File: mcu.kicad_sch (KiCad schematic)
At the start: 16 parts, among them J301 Conn_PIC_ICSP_ICD, U301 LM4040DBZ-2.0, U302 PIC18F24K42

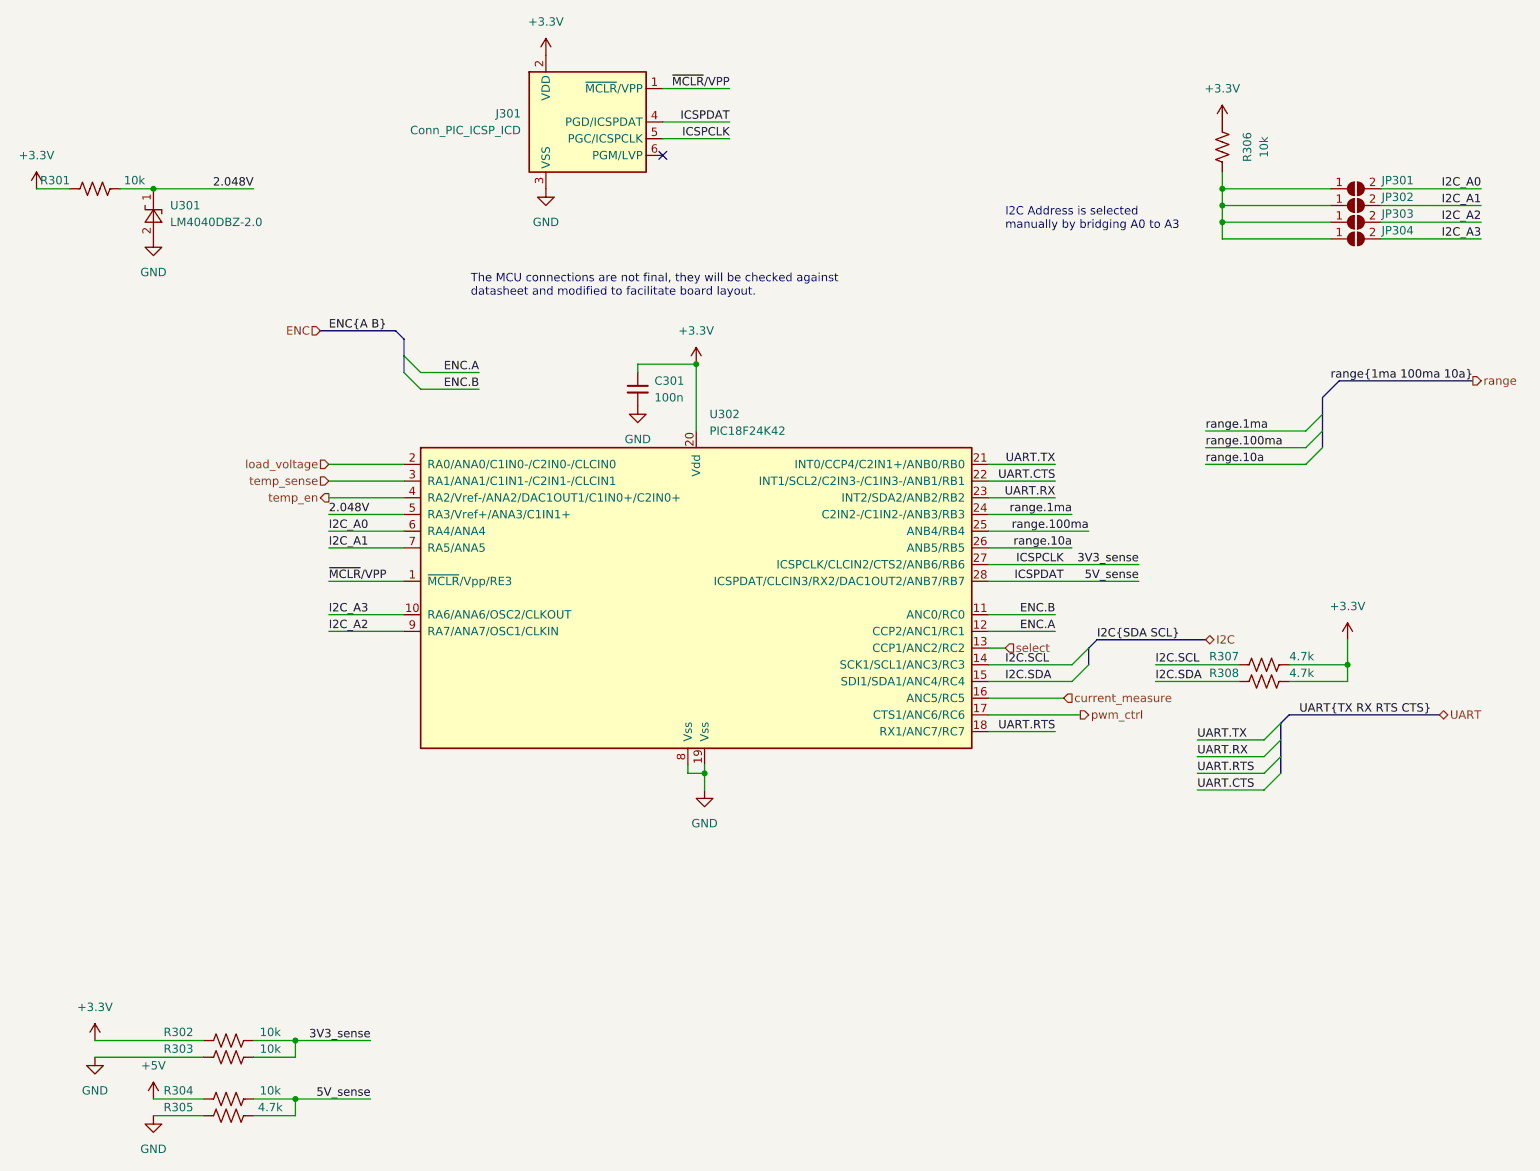
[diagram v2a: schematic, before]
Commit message: Add partnumbers
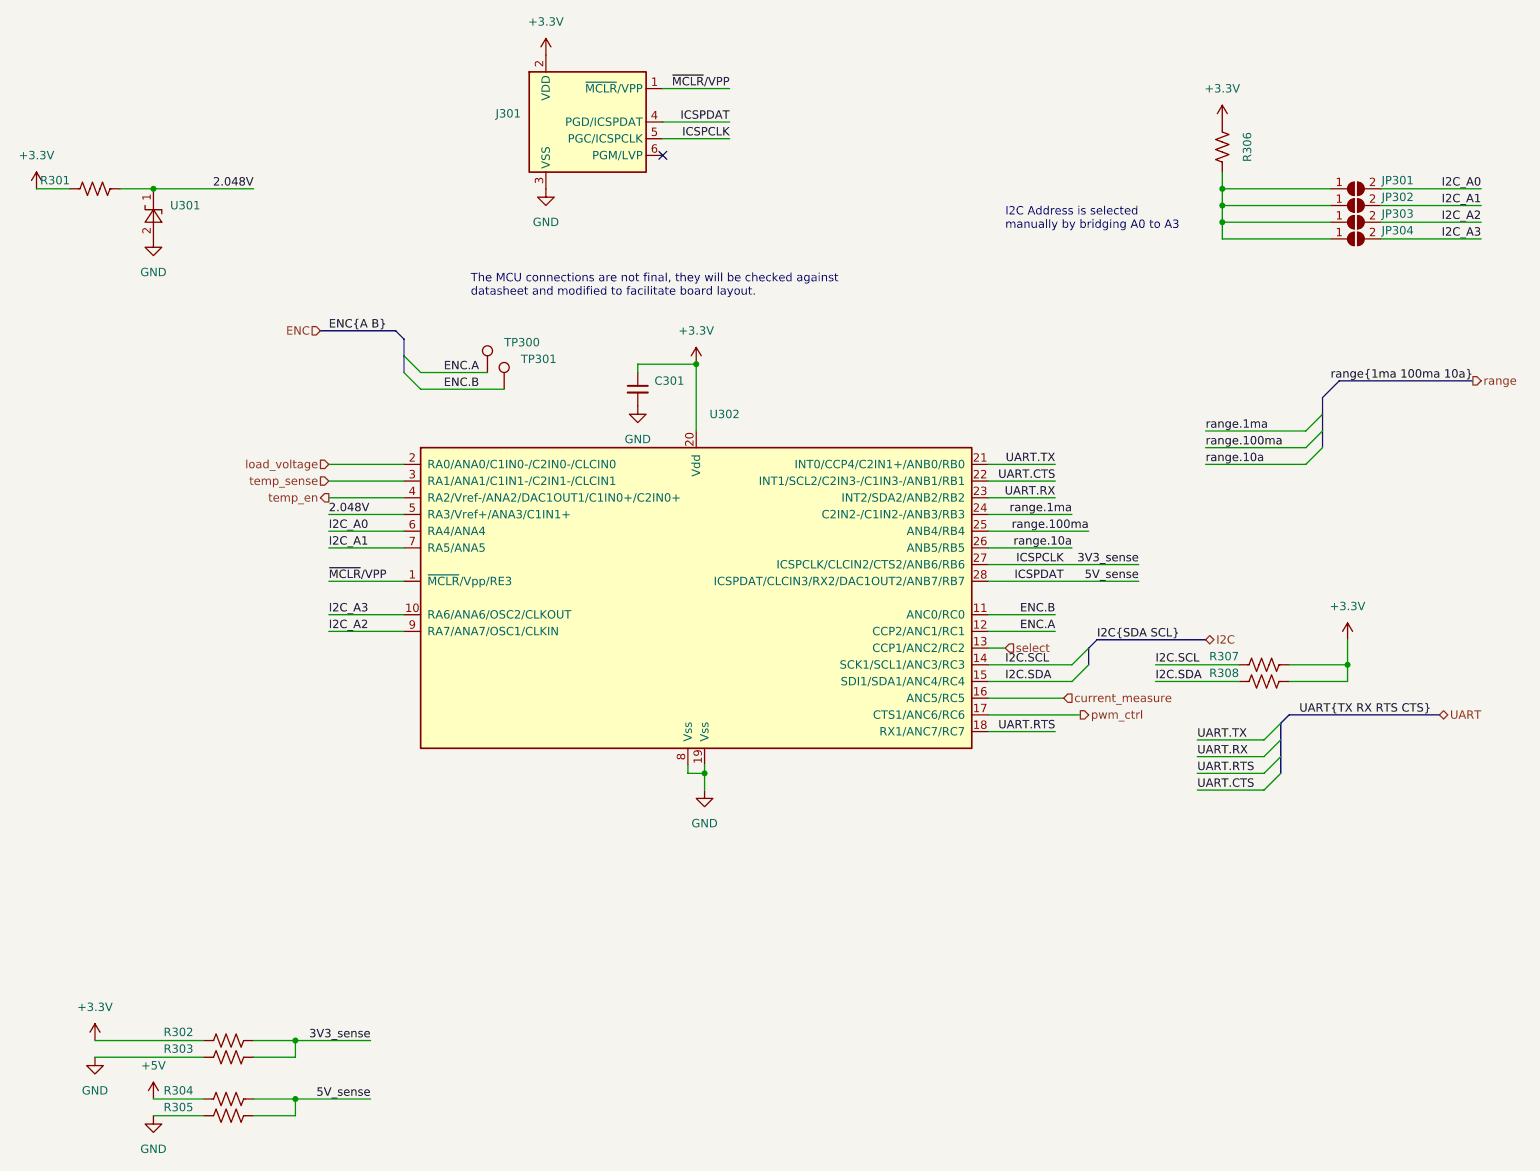
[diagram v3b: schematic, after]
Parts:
- added TP300, TP301: (no value), symbol Connector:TestPoint
- C301: value 100n -> (none); footprint Capacitor_SMD:C_0402_1005Metric -> (none); Manufacturer (none) -> Generic; PartNumber (none) -> Generic
- J301: value Conn_PIC_ICSP_ICD -> (none); footprint Connector_PinHeader_2.54mm:PinHeader_1x06_P2.54mm_Vertical -> (none); Manufacturer (none) -> Generic; PartNumber (none) -> Generic
- JP301, JP302, JP303, JP304: value SB -> (none); footprint Jumper:SolderJumper-2_P1.3mm_Open_TrianglePad1.0x1.5mm -> (none); Manufacturer (none) -> N.A.; PartNumber (none) -> N.A.
- R301, R302, R303, R304, R306: value 10k -> (none); footprint Resistor_SMD:R_0805_2012Metric -> (none); Manufacturer (none) -> Generic; PartNumber (none) -> Generic
- R305, R307, R308: value 4.7k -> (none); footprint Resistor_SMD:R_0805_2012Metric -> (none); Manufacturer (none) -> Generic; PartNumber (none) -> Generic
- U301: value LM4040DBZ-2.0 -> (none); footprint Package_TO_SOT_SMD:SOT-23 -> (none); Manufacturer (none) -> Texas Instruments; PartNumber (none) -> LM4040DBZ-2.0
- U302: value PIC18F24K42 -> (none); footprint Package_SO:SSOP-28_5.3x10.2mm_P0.65mm -> (none)
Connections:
- net ENC.A: now also TP300.1
- net ENC.B: now also TP301.1

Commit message: Fix missing footprints in schematic
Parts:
- C301, J301, JP301, JP302, JP303, JP304, R301, R302, R303, R304, R305, R306, R307, R308, TP300, TP301: now left out of the parts list
- U301: PartNumber LM4040DBZ-2.0 -> LM4040C20IDBZ
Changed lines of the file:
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@@
   )
   (symbol (lib_id "Device:R_US") (at 228.6 115.57 270) (unit 1)
-    (in_bom yes) (on_board yes)
+    (in_bom no) (on_board yes)
     (property "Reference" "R308" (id 0) (at 224.79 114.3 90)
       (effects (font (size 1.27 1.27)) (justify right))
@@
   )
   (symbol (lib_id "Device:R_US") (at 50.8 40.64 270) (unit 1)
-    (in_bom yes) (on_board yes)
+    (in_bom no) (on_board yes)
     (property "Reference" "R301" (id 0) (at 46.99 39.37 90)
       (effects (font (size 1.27 1.27)) (justify right))
@@
   )
   (symbol (lib_id "Connector:TestPoint") (at 110.49 68.58 0) (unit 1)
-    (in_bom yes) (on_board yes) (fields_autoplaced)
+    (in_bom no) (on_board yes) (fields_autoplaced)
     (property "Reference" "TP300" (id 0) (at 113.03 64.0079 0)
       (effects (font (size 1.27 1.27)) (justify left))
@@
   )
   (symbol (lib_id "Connector:Conn_PIC_ICSP_ICD") (at 124.46 30.48 0) (unit 1)
-    (in_bom yes) (on_board yes) (fields_autoplaced)
+    (in_bom no) (on_board yes) (fields_autoplaced)
     (property "Reference" "J301" (id 0) (at 115.57 29.2099 0)
       (effects (font (size 1.27 1.27)) (justify right))
@@
   )
   (symbol (lib_id "Device:R_US") (at 71.12 170.18 270) (unit 1)
-    (in_bom yes) (on_board yes)
+    (in_bom no) (on_board yes)
     (property "Reference" "R302" (id 0) (at 63.5 168.91 90))
     (property "Value" "" (id 1) (at 77.47 168.91 90))
@@
   )
   (symbol (lib_id "Jumper:SolderJumper_2_Open") (at 242.57 40.64 0) (unit 1)
-    (in_bom yes) (on_board yes)
+    (in_bom no) (on_board yes)
     (property "Reference" "JP301" (id 0) (at 248.92 39.37 0))
     (property "Value" "" (id 1) (at 242.57 36.83 0)
@@
   )
   (symbol (lib_id "Device:R_US") (at 71.12 172.72 90) (unit 1)
-    (in_bom yes) (on_board yes)
+    (in_bom no) (on_board yes)
     (property "Reference" "R303" (id 0) (at 63.5 171.45 90))
     (property "Value" "" (id 1) (at 77.47 171.45 90))
@@
   )
   (symbol (lib_id "Connector:TestPoint") (at 113.03 71.12 0) (unit 1)
-    (in_bom yes) (on_board yes) (fields_autoplaced)
+    (in_bom no) (on_board yes) (fields_autoplaced)
     (property "Reference" "TP301" (id 0) (at 115.57 66.5479 0)
       (effects (font (size 1.27 1.27)) (justify left))
@@
   )
   (symbol (lib_id "Device:R_US") (at 71.12 179.07 270) (unit 1)
-    (in_bom yes) (on_board yes)
+    (in_bom no) (on_board yes)
     (property "Reference" "R304" (id 0) (at 63.5 177.8 90))
     (property "Value" "" (id 1) (at 77.47 177.8 90))
@@
       (effects (font (size 1.27 1.27)) hide)
     )
-    (property "PartNumber" "LM4040DBZ-2.0" (id 5) (at 59.69 44.45 0)
+    (property "PartNumber" "LM4040C20IDBZ" (id 5) (at 59.69 44.45 0)
       (effects (font (size 1.27 1.27)) hide)
     )
@@
   )
   (symbol (lib_id "Device:C_Small") (at 133.35 71.12 0) (unit 1)
-    (in_bom yes) (on_board yes) (fields_autoplaced)
+    (in_bom no) (on_board yes) (fields_autoplaced)
     (property "Reference" "C301" (id 0) (at 135.89 69.8562 0)
       (effects (font (size 1.27 1.27)) (justify left))
@@
   )
   (symbol (lib_id "Device:R_US") (at 222.25 34.29 180) (unit 1)
-    (in_bom yes) (on_board yes)
+    (in_bom no) (on_board yes)
     (property "Reference" "R306" (id 0) (at 226.06 34.29 90))
     (property "Value" "" (id 1) (at 228.6 34.29 90))
@@
   )
   (symbol (lib_id "Device:R_US") (at 228.6 113.03 270) (unit 1)
-    (in_bom yes) (on_board yes)
+    (in_bom no) (on_board yes)
     (property "Reference" "R307" (id 0) (at 224.79 111.76 90)
       (effects (font (size 1.27 1.27)) (justify right))
@@
   )
   (symbol (lib_id "Jumper:SolderJumper_2_Open") (at 242.57 45.72 0) (unit 1)
-    (in_bom yes) (on_board yes)
+    (in_bom no) (on_board yes)
     (property "Reference" "JP303" (id 0) (at 248.92 44.45 0))
     (property "Value" "" (id 1) (at 242.57 41.91 0)
@@
   )
   (symbol (lib_id "Jumper:SolderJumper_2_Open") (at 242.57 48.26 0) (unit 1)
-    (in_bom yes) (on_board yes)
+    (in_bom no) (on_board yes)
     (property "Reference" "JP304" (id 0) (at 248.92 46.99 0))
     (property "Value" "" (id 1) (at 242.57 44.45 0)
@@
   )
   (symbol (lib_id "Jumper:SolderJumper_2_Open") (at 242.57 43.18 0) (unit 1)
-    (in_bom yes) (on_board yes)
+    (in_bom no) (on_board yes)
     (property "Reference" "JP302" (id 0) (at 248.92 41.91 0))
     (property "Value" "" (id 1) (at 242.57 39.37 0)
@@
   )
   (symbol (lib_id "Device:R_US") (at 71.12 181.61 90) (unit 1)
-    (in_bom yes) (on_board yes)
+    (in_bom no) (on_board yes)
     (property "Reference" "R305" (id 0) (at 63.5 180.34 90))
     (property "Value" "" (id 1) (at 77.47 180.34 90))

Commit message: Add feedback resistors for regulator
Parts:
- U301: PartNumber LM4040C20IDBZ -> LM4040C20QDBZT
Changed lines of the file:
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@@
       (effects (font (size 1.27 1.27)) hide)
     )
-    (property "PartNumber" "LM4040C20IDBZ" (id 5) (at 59.69 44.45 0)
+    (property "PartNumber" "LM4040C20QDBZT" (id 5) (at 59.69 44.45 0)
       (effects (font (size 1.27 1.27)) hide)
     )
